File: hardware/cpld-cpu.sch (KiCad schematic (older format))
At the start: 433 parts, among them J1 Acc, J10 Page, J11 PC_H, J12 Conn_02x14_Odd_Even, J13 GPIO, J14 Conn_02x17_Odd_Even, J2 X, J3 IR, J4 AXM, J5 Dec, J6 AR, J7 ALU, J8 Index, J9 PC_L, SW1 BTN0, SW2 BTN1, SW3 BTN2, U1 Acc, U10 RAM_Page, U11 PC_H, U12 CY62138FV30LL, U13 GPIO_RNG, U2 X, U3 IR, U4 Multiplexer, U5 Decoder, U6 AR, U7 ALU, U8 RAM_Index, U9 PC_L

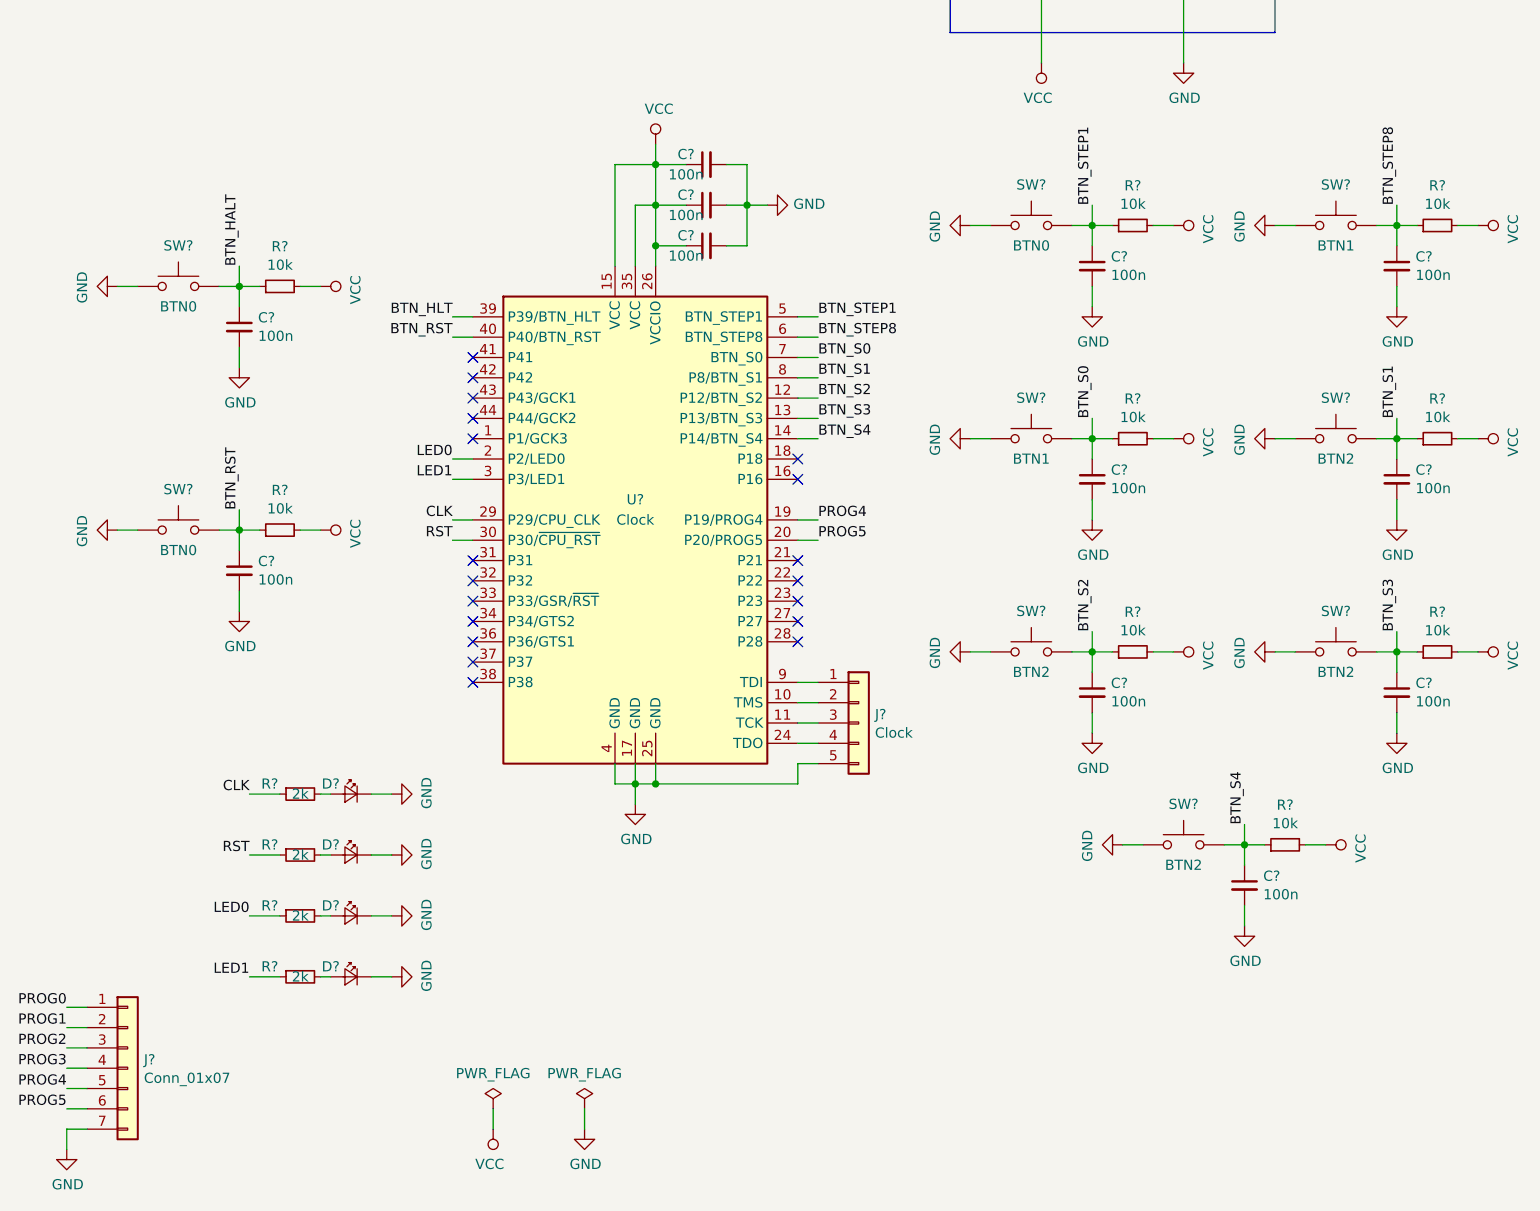
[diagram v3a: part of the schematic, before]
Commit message: Clock routing
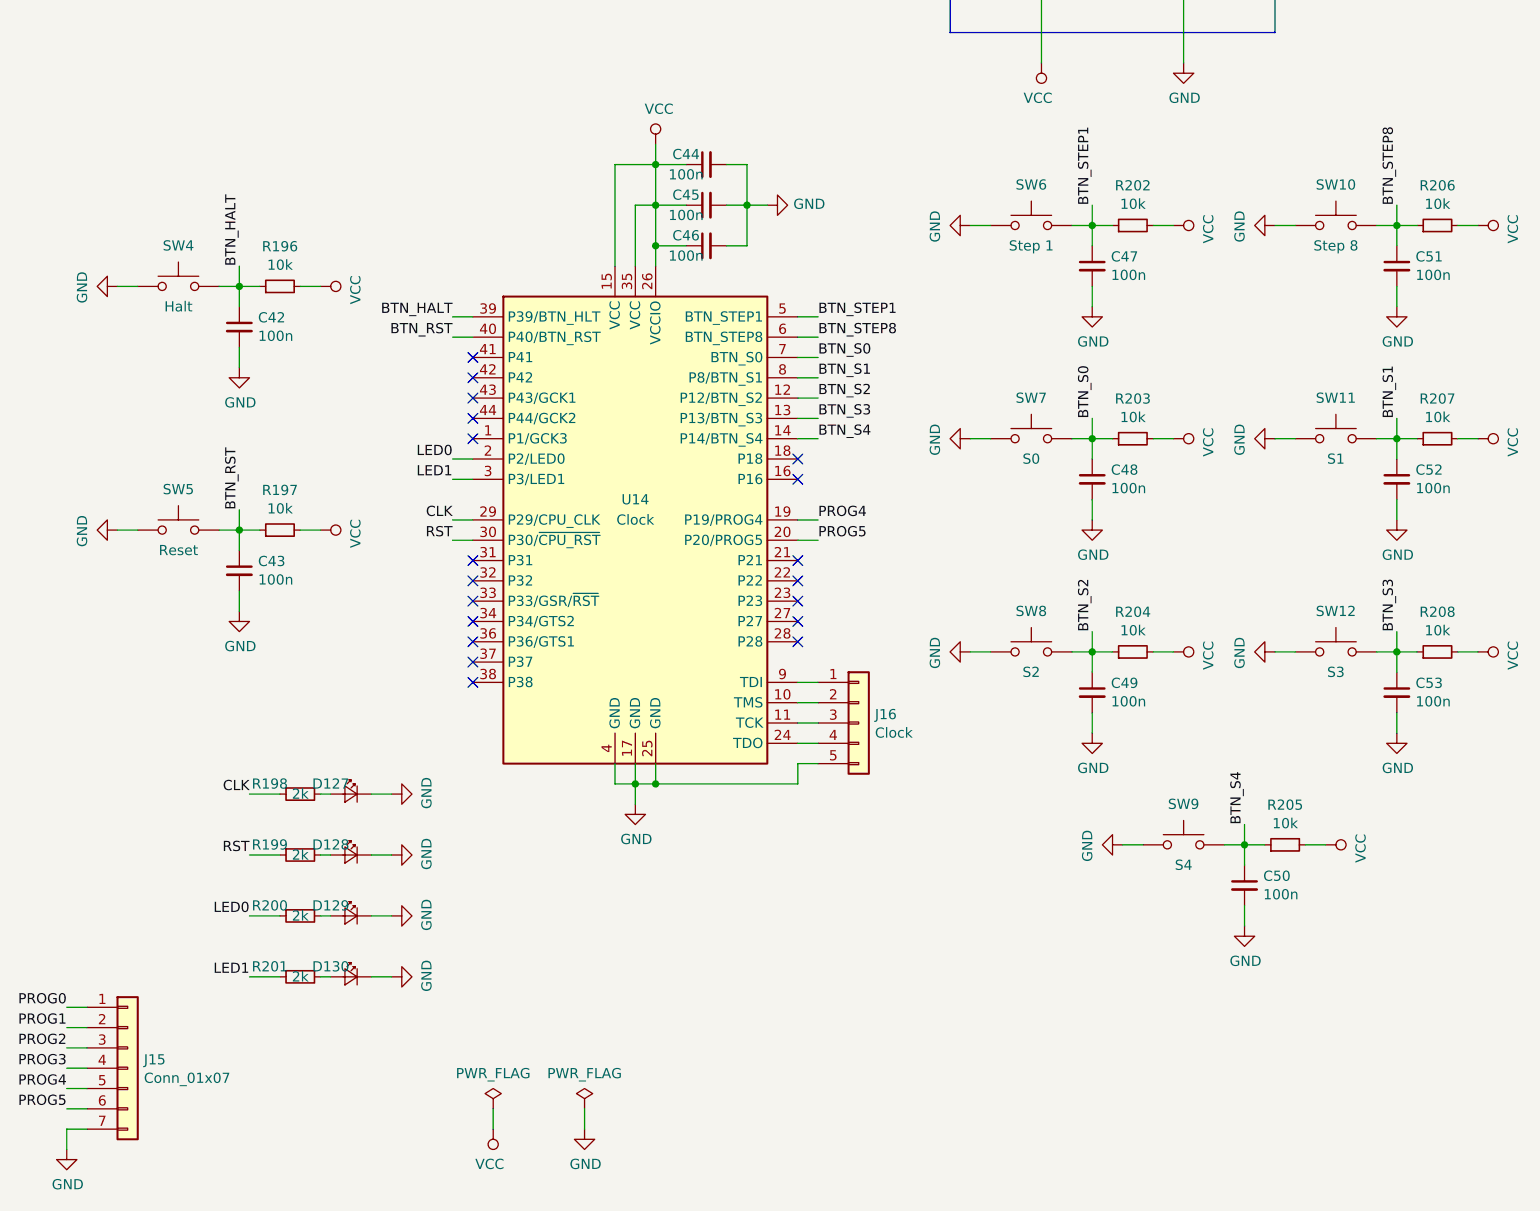
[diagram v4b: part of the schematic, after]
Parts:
- J15: renamed from J?; footprint (none) -> Pin_Headers:Pin_Header_Straight_1x07_Pitch2.54mm
- SW10: renamed from SW?; value BTN1 -> Step 8
- SW11: renamed from SW?; value BTN2 -> S1
- SW12: renamed from SW?; value BTN2 -> S3
- SW4: renamed from SW?; value BTN0 -> Halt
- SW5: renamed from SW?; value BTN0 -> Reset
- SW6: renamed from SW?; value BTN0 -> Step 1
- SW7: renamed from SW?; value BTN1 -> S0
- SW8: renamed from SW?; value BTN2 -> S2
- SW9: renamed from SW?; value BTN2 -> S4
- gave numbers to parts that had none: 31
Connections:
- net BTN_HLT is gone; now on net BTN_HALT: U14.39 (P39/BTN_HLT)

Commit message: Finished ratsnest
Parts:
- added D131: LED_Small, LEDs:LED_0805_HandSoldering, symbol Device:LED_Small
- added R209: 2k, Resistors_SMD:R_0805_HandSoldering, symbol Device:R_Small
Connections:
- net A_CC: now also R209.1
- net GND: now also D131.1 (K)
- new net: D131.2 (A), R209.2
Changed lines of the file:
@@
 L power:GND #PWR01
 U 1 1 79E93F96
-P 1250 10450
-F 0 "#PWR01" H 1250 10200 50  0001 C CNN
-F 1 "GND" H 1255 10277 50  0000 C CNN
-F 2 "" H 1250 10450 50  0001 C CNN
-F 3 "" H 1250 10450 50  0001 C CNN
-	1    1250 10450
+P 1250 10700
+F 0 "#PWR01" H 1250 10450 50  0001 C CNN
+F 1 "GND" H 1255 10527 50  0000 C CNN
+F 2 "" H 1250 10700 50  0001 C CNN
+F 3 "" H 1250 10700 50  0001 C CNN
+	1    1250 10700
 	1    0    0    -1
 $EndComp
@@
 D3
 Wire Wire Line
-	2050 3750 2350 3750
-Wire Bus Line
-	2300 3050 2300 4650
-Wire Bus Line
-	2300 4750 2300 7900
-Wire Wire Line
 	9300 4550 9300 7700
 Wire Wire Line
@@
 Wire Wire Line
 	20750 15450 20650 15450
-Wire Bus Line
-	26600 9800 26600 10150
-Wire Wire Line
-	2050 7700 2750 7700
-Wire Wire Line
-	2050 7400 2950 7400
-Wire Wire Line
-	2050 7800 2700 7800
-Wire Wire Line
-	2050 7600 2800 7600
-Wire Wire Line
-	2050 7500 2850 7500
-Wire Wire Line
-	2050 7300 2950 7300
-Wire Wire Line
-	2050 7200 2950 7200
-Wire Wire Line
-	2050 3550 2750 3550
-Wire Wire Line
-	2050 3250 2950 3250
+$Comp
+L Device:LED_Small D131
+U 1 1 5C51519A
+P 1400 10450
+F 0 "D131" H 1500 10500 50  0000 C CNN
+F 1 "LED_Small" H 1400 10594 50  0001 C CNN
+F 2 "LEDs:LED_0805_HandSoldering" V 1400 10450 50  0001 C CNN
+F 3 "~" V 1400 10450 50  0001 C CNN
+	1    1400 10450
+	1    0    0    -1
+$EndComp
+$Comp
+L Device:R_Small R209
+U 1 1 5C5151A1
+P 1650 10450
+F 0 "R209" V 1600 10600 50  0000 C CNN
+F 1 "2k" V 1650 10450 50  0000 C CNN
+F 2 "Resistors_SMD:R_0805_HandSoldering" H 1650 10450 50  0001 C CNN
+F 3 "~" H 1650 10450 50  0001 C CNN
+	1    1650 10450
+	0    1    1    0
+$EndComp
 Wire Wire Line
-	2050 3650 2700 3650
+	1550 10450 1500 10450
 Wire Wire Line
-	2050 3450 2800 3450
+	1300 10450 1250 10450
+Entry Wire Line
+	2800 10450 2900 10550
 Wire Wire Line
-	2050 3350 2850 3350
+	1750 10450 2800 10450
+Text Label 2100 10450 0    50   ~ 0
+A_CC
 Wire Wire Line
-	2050 3150 2950 3150
+	1250 10700 1250 10450
+Connection ~ 1250 10450
 Wire Wire Line
-	2050 3050 2950 3050
+	2050 3750 2350 3750
+Wire Bus Line
+	26600 9800 26600 10150
 Wire Wire Line
 	11050 7200 12100 7200
@@
 Wire Bus Line
 	14950 7200 14950 9150
+Wire Wire Line
+	2050 3050 2950 3050
+Wire Wire Line
+	2050 3150 2950 3150
+Wire Wire Line
+	2050 3350 2850 3350
+Wire Wire Line
+	2050 3450 2800 3450
+Wire Wire Line
+	2050 3650 2700 3650
+Wire Wire Line
+	2050 3250 2950 3250
+Wire Wire Line
+	2050 3550 2750 3550
+Wire Wire Line
+	2050 7200 2950 7200
+Wire Wire Line
+	2050 7300 2950 7300
+Wire Wire Line
+	2050 7500 2850 7500
+Wire Wire Line
+	2050 7600 2800 7600
+Wire Wire Line
+	2050 7800 2700 7800
+Wire Wire Line
+	2050 7400 2950 7400
+Wire Wire Line
+	2050 7700 2750 7700
 Wire Bus Line
 	14550 2650 14550 4850
@@
 	19100 1800 19100 4250
 Wire Bus Line
+	2900 9900 2900 12050
+Wire Bus Line
+	2300 3050 2300 4650
+Wire Bus Line
+	2300 4750 2300 7900
+Wire Bus Line
 	11300 6000 11300 9150
 Wire Bus Line
@@
 	2350 11250 2350 14350
 Wire Bus Line
-	2900 9900 2900 12050
-Wire Bus Line
 	6750 850  6750 3750

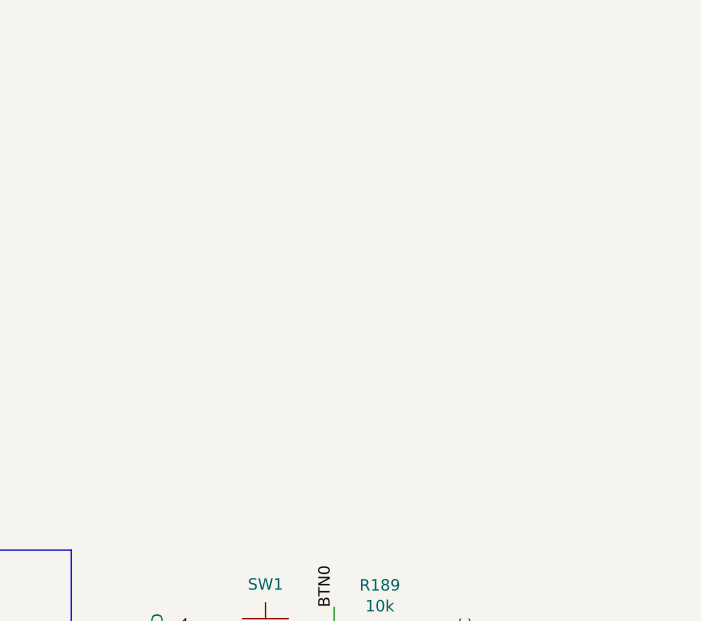
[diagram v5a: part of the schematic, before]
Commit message: Add logos and version
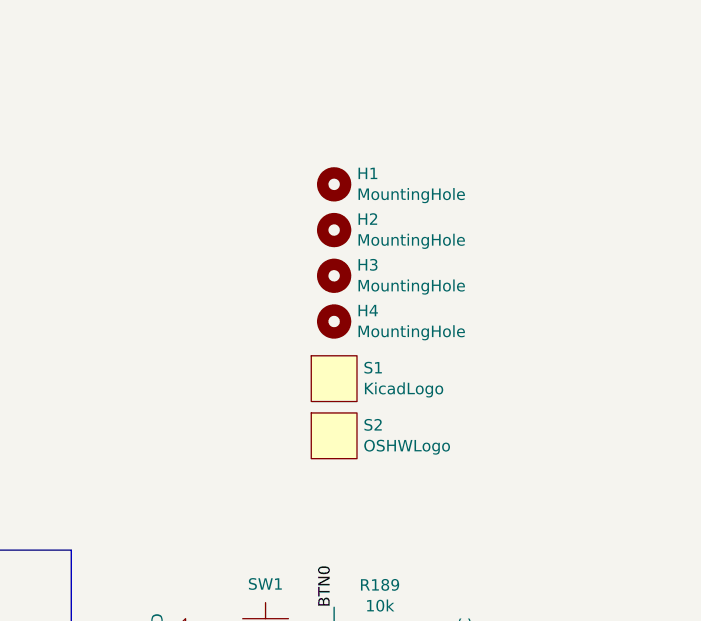
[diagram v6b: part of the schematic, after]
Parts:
- added H1, H2, H3, H4: MountingHole, Mounting_Holes:MountingHole_4.3mm_M4, symbol Mechanical:MountingHole
- added S1: KicadLogo, Symbols:Symbol_KiCAD-Logo_CopperAndSilkScreenTop, symbol CPLD_CPU_Symbols:KicadLogo
- added S2: OSHWLogo, CPLD_CPU_Symbols:OSHW-Logo2_14.6x12mm_Copper_Top, symbol CPLD_CPU_Symbols:OSHWLogo
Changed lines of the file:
@@
 	2050 3750 2350 3750
 Wire Bus Line
+	2300 3050 2300 4650
+Wire Bus Line
+	2300 4750 2300 7900
+$Comp
+L Mechanical:MountingHole H4
+U 1 1 5C519B71
+P 26300 3900
+F 0 "H4" H 26400 3946 50  0000 L CNN
+F 1 "MountingHole" H 26400 3855 50  0000 L CNN
+F 2 "Mounting_Holes:MountingHole_4.3mm_M4" H 26300 3900 50  0001 C CNN
+F 3 "~" H 26300 3900 50  0001 C CNN
+	1    26300 3900
+	1    0    0    -1
+$EndComp
+$Comp
+L Mechanical:MountingHole H3
+U 1 1 5C85F760
+P 26300 3700
+F 0 "H3" H 26400 3746 50  0000 L CNN
+F 1 "MountingHole" H 26400 3655 50  0000 L CNN
+F 2 "Mounting_Holes:MountingHole_4.3mm_M4" H 26300 3700 50  0001 C CNN
+F 3 "~" H 26300 3700 50  0001 C CNN
+	1    26300 3700
+	1    0    0    -1
+$EndComp
+$Comp
+L Mechanical:MountingHole H2
+U 1 1 5C85FADE
+P 26300 3500
+F 0 "H2" H 26400 3546 50  0000 L CNN
+F 1 "MountingHole" H 26400 3455 50  0000 L CNN
+F 2 "Mounting_Holes:MountingHole_4.3mm_M4" H 26300 3500 50  0001 C CNN
+F 3 "~" H 26300 3500 50  0001 C CNN
+	1    26300 3500
+	1    0    0    -1
+$EndComp
+$Comp
+L Mechanical:MountingHole H1
+U 1 1 5C85FE62
+P 26300 3300
+F 0 "H1" H 26400 3346 50  0000 L CNN
+F 1 "MountingHole" H 26400 3255 50  0000 L CNN
+F 2 "Mounting_Holes:MountingHole_4.3mm_M4" H 26300 3300 50  0001 C CNN
+F 3 "~" H 26300 3300 50  0001 C CNN
+	1    26300 3300
+	1    0    0    -1
+$EndComp
+$Comp
+L CPLD_CPU_Symbols:KicadLogo S1
+U 1 1 5CEF5532
+P 26650 4150
+F 0 "S1" H 26428 4196 50  0000 L CNN
+F 1 "KicadLogo" H 26428 4105 50  0000 L CNN
+F 2 "Symbols:Symbol_KiCAD-Logo_CopperAndSilkScreenTop" H 26650 4150 50  0001 C CNN
+F 3 "" H 26650 4150 50  0001 C CNN
+	1    26650 4150
+	1    0    0    -1
+$EndComp
+Wire Bus Line
 	26600 9800 26600 10150
 Wire Wire Line
@@
 Wire Bus Line
 	11650 6700 11650 8900
+Wire Wire Line
+	2050 3050 2950 3050
+Wire Wire Line
+	2050 3150 2950 3150
+Wire Wire Line
+	2050 3350 2850 3350
+Wire Wire Line
+	2050 3450 2800 3450
+Wire Wire Line
+	2050 3650 2700 3650
+Wire Wire Line
+	2050 3250 2950 3250
+Wire Wire Line
+	2050 3550 2750 3550
+Wire Wire Line
+	2050 7200 2950 7200
+Wire Wire Line
+	2050 7300 2950 7300
+Wire Wire Line
+	2050 7500 2850 7500
+Wire Wire Line
+	2050 7600 2800 7600
+Wire Wire Line
+	2050 7800 2700 7800
+Wire Wire Line
+	2050 7400 2950 7400
+Wire Wire Line
+	2050 7700 2750 7700
 Wire Bus Line
 	10550 12050 10550 14350
@@
 Wire Bus Line
 	14950 7200 14950 9150
-Wire Wire Line
-	2050 3050 2950 3050
-Wire Wire Line
-	2050 3150 2950 3150
-Wire Wire Line
-	2050 3350 2850 3350
-Wire Wire Line
-	2050 3450 2800 3450
-Wire Wire Line
-	2050 3650 2700 3650
-Wire Wire Line
-	2050 3250 2950 3250
-Wire Wire Line
-	2050 3550 2750 3550
-Wire Wire Line
-	2050 7200 2950 7200
-Wire Wire Line
-	2050 7300 2950 7300
-Wire Wire Line
-	2050 7500 2850 7500
-Wire Wire Line
-	2050 7600 2800 7600
-Wire Wire Line
-	2050 7800 2700 7800
-Wire Wire Line
-	2050 7400 2950 7400
-Wire Wire Line
-	2050 7700 2750 7700
 Wire Bus Line
 	14550 2650 14550 4850
@@
 	2900 9900 2900 12050
 Wire Bus Line
-	2300 3050 2300 4650
-Wire Bus Line
-	2300 4750 2300 7900
-Wire Bus Line
 	11300 6000 11300 9150
 Wire Bus Line
@@
 Wire Bus Line
 	18800 6500 18800 9150
+$Comp
+L CPLD_CPU_Symbols:OSHWLogo S2
+U 1 1 5D23BE06
+P 26650 4400
+F 0 "S2" H 26428 4446 50  0000 L CNN
+F 1 "OSHWLogo" H 26428 4355 50  0000 L CNN
+F 2 "CPLD_CPU_Symbols:OSHW-Logo2_14.6x12mm_Copper_Top" H 26650 4400 50  0001 C CNN
+F 3 "" H 26650 4400 50  0001 C CNN
+	1    26650 4400
+	1    0    0    -1
+$EndComp
 $EndSCHEMATC
